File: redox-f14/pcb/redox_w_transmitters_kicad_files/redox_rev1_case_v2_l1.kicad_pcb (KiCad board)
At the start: 2 copper layers, 164.3 x 134.8 mm, 0 parts

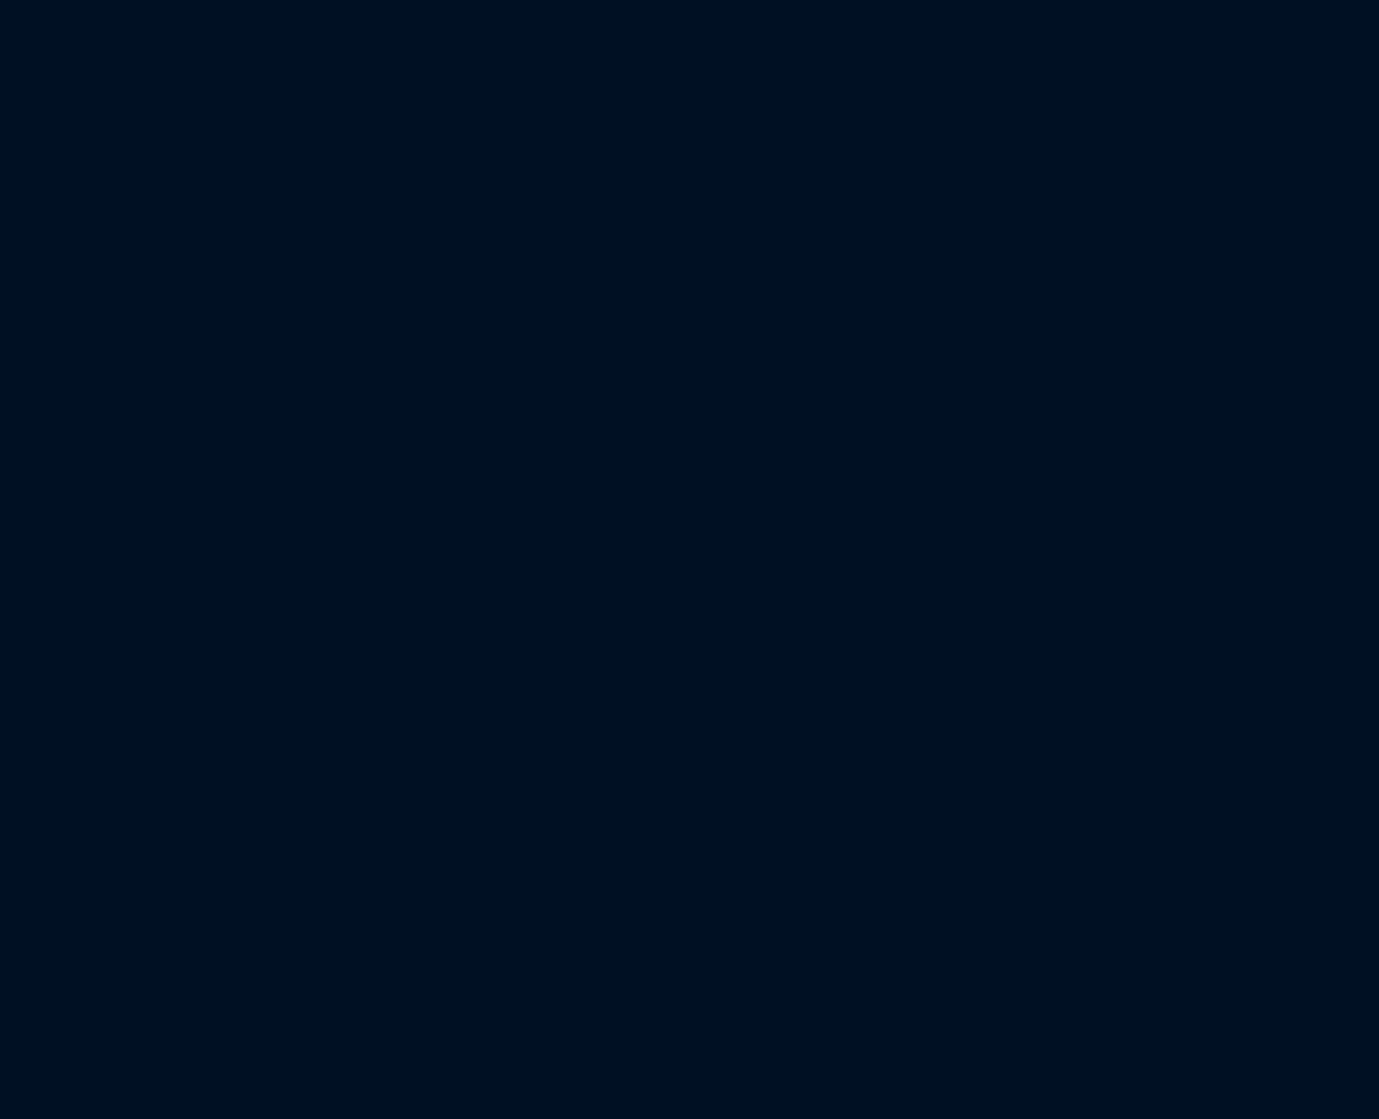
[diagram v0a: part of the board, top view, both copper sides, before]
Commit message: wingxx case update
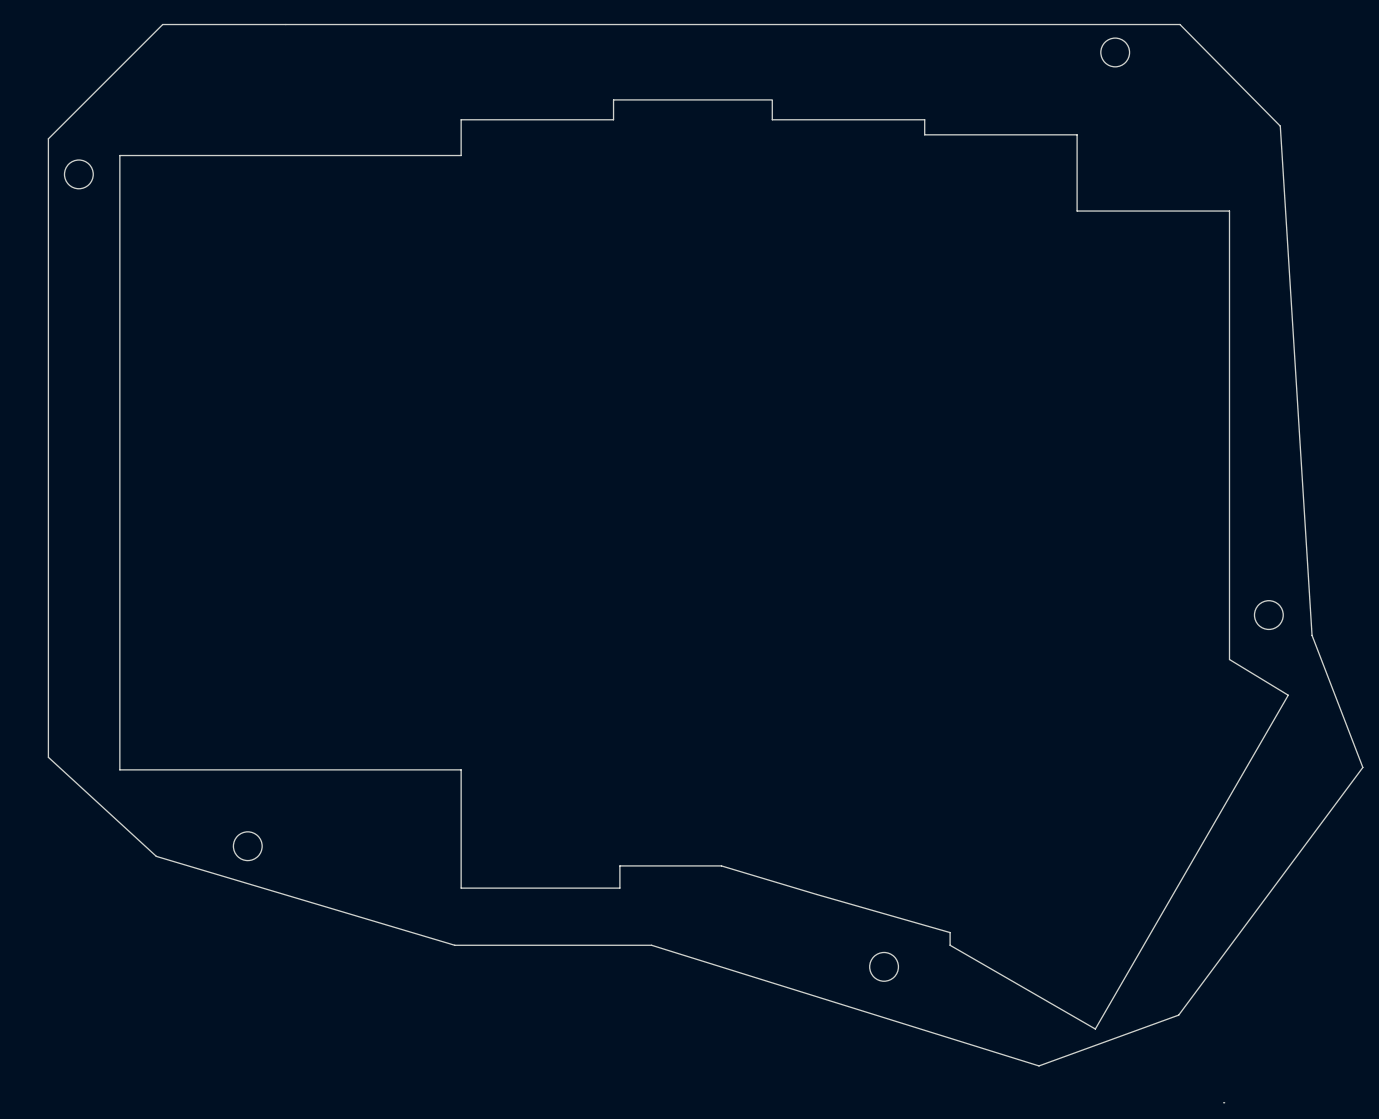
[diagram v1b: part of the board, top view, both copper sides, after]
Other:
- board size 164.3 x 134.8 mm -> 377.9 x 135.8 mm
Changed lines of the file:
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@@
   (general
     (thickness 1.6)
-    (drawings 43)
+    (drawings 86)
     (tracks 0)
     (zones 0)
@@
     (visible_elements 7FFFFFFF)
     (pcbplotparams
-      (layerselection 0x010fc_ffffffff)
+      (layerselection 0x01000_7ffffffe)
       (usegerberextensions true)
       (usegerberattributes false)
       (usegerberadvancedattributes false)
       (creategerberjobfile false)
-      (excludeedgelayer true)
+      (excludeedgelayer false)
       (linewidth 0.100000)
       (plotframeref false)
@@
       (psnegative false)
       (psa4output false)
-      (plotreference true)
-      (plotvalue true)
+      (plotreference false)
+      (plotvalue false)
       (plotinvisibletext false)
-      (padsonsilk false)
+      (padsonsilk true)
       (subtractmaskfromsilk false)
-      (outputformat 1)
+      (outputformat 3)
       (mirror false)
       (drillshape 0)
       (scaleselection 1)
-      (outputdirectory "gerber_files/"))
+      (outputdirectory "dxf/"))
   )
   (net 0 "")
@@
     (uvia_drill 0.1)
   )
+  (gr_circle (center 417.60775 44.98975) (end 418.87775 46.25975) (layer Edge.Cuts) (width 0.1))
+  (gr_circle (center 436.8165 115.316) (end 438.0865 116.586) (layer Edge.Cuts) (width 0.1))
+  (gr_circle (center 388.71525 159.28975) (end 389.98525 160.55975) (layer Edge.Cuts) (width 0.1))
+  (gr_circle (center 309.1815 144.2085) (end 310.4515 145.4785) (layer Edge.Cuts) (width 0.1))
+  (gr_circle (center 288.06775 60.22975) (end 289.33775 61.49975) (layer Edge.Cuts) (width 0.1))
+  (gr_line (start 354.9015 53.4035) (end 354.9015 50.92225) (layer Edge.Cuts) (width 0.1))
+  (gr_line (start 284.25775 55.78475) (end 284.25775 133.096) (layer Edge.Cuts) (width 0.1))
+  (gr_line (start 293.189 57.87225) (end 335.8515 57.87225) (layer Edge.Cuts) (width 0.1))
+  (gr_line (start 374.74525 51.02225) (end 374.74525 53.4035) (layer Edge.Cuts) (width 0.1))
+  (gr_line (start 335.8515 134.666) (end 293.189 134.666) (layer Edge.Cuts) (width 0.1))
+  (gr_line (start 412.84525 55.28475) (end 412.84525 64.80975) (layer Edge.Cuts) (width 0.1))
+  (gr_line (start 335.05775 156.591) (end 297.7515 145.4785) (layer Edge.Cuts) (width 0.1))
+  (gr_line (start 380.3015 150.241) (end 368.39525 146.67225) (layer Edge.Cuts) (width 0.1))
+  (gr_line (start 297.7515 145.4785) (end 284.25775 133.096) (layer Edge.Cuts) (width 0.1))
+  (gr_line (start 284.25775 55.78475) (end 298.54525 41.49725) (layer Edge.Cuts) (width 0.1))
+  (gr_line (start 355.69525 149.44725) (end 355.69525 146.67225) (layer Edge.Cuts) (width 0.1))
+  (gr_line (start 380.3015 150.241) (end 396.97025 155.0035) (layer Edge.Cuts) (width 0.1))
+  (gr_line (start 374.74525 53.4035) (end 393.79525 53.4035) (layer Edge.Cuts) (width 0.1))
+  (gr_line (start 335.8515 149.44725) (end 355.69525 149.44725) (layer Edge.Cuts) (width 0.1))
+  (gr_line (start 293.189 134.666) (end 293.189 57.87225) (layer Edge.Cuts) (width 0.1))
+  (gr_line (start 354.9015 50.92225) (end 374.74525 50.92225) (layer Edge.Cuts) (width 0.1))
+  (gr_line (start 335.8515 57.87225) (end 335.8515 53.4035) (layer Edge.Cuts) (width 0.1))
+  (gr_line (start 393.79525 55.28475) (end 393.79525 53.4035) (layer Edge.Cuts) (width 0.1))
+  (gr_line (start 335.8515 53.4035) (end 354.9015 53.4035) (layer Edge.Cuts) (width 0.1))
+  (gr_line (start 335.8515 149.44725) (end 335.8515 134.666) (layer Edge.Cuts) (width 0.1))
+  (gr_line (start 393.79525 55.28475) (end 412.84525 55.28475) (layer Edge.Cuts) (width 0.1))
+  (gr_line (start 425.54525 165.32225) (end 408.08275 171.67225) (layer Edge.Cuts) (width 0.1))
+  (gr_line (start 408.08275 171.67225) (end 359.664 156.591) (layer Edge.Cuts) (width 0.1))
+  (gr_line (start 359.664 156.591) (end 335.05775 156.591) (layer Edge.Cuts) (width 0.1))
+  (gr_line (start 355.69525 146.67225) (end 368.39525 146.67225) (layer Edge.Cuts) (width 0.1))
+  (gr_line (start 442.214 117.856) (end 448.564 134.366) (layer Edge.Cuts) (width 0.1))
+  (gr_line (start 448.564 134.366) (end 425.54525 165.32225) (layer Edge.Cuts) (width 0.1))
+  (gr_line (start 438.24525 54.19725) (end 442.214 117.856) (layer Edge.Cuts) (width 0.1))
+  (gr_line (start 431.165 176.276) (end 431.292 176.276) (angle 90) (layer Edge.Cuts) (width 0.1))
+  (gr_line (start 425.704 41.49725) (end 438.24525 54.19725) (layer Edge.Cuts) (width 0.1))
+  (gr_line (start 298.54525 41.49725) (end 313.944 41.49725) (layer Edge.Cuts) (width 0.1))
+  (gr_line (start 313.944 41.49725) (end 425.704 41.49725) (layer Edge.Cuts) (width 0.1))
+  (gr_line (start 415.1265 167.05975) (end 396.97025 156.591) (layer Edge.Cuts) (width 0.1))
+  (gr_line (start 396.97025 156.591) (end 396.97025 155.0035) (layer Edge.Cuts) (width 0.1))
+  (gr_line (start 412.84525 64.80975) (end 431.89525 64.80975) (layer Edge.Cuts) (width 0.1))
+  (gr_line (start 431.89525 64.80975) (end 431.89525 120.87225) (layer Edge.Cuts) (width 0.1))
+  (gr_line (start 431.89525 120.87225) (end 439.239 125.33475) (layer Edge.Cuts) (width 0.1))
+  (gr_line (start 439.239 125.33475) (end 415.1265 167.05975) (layer Edge.Cuts) (width 0.1))
   (gr_circle (center 203.99375 43.97375) (end 205.26375 43.97375) (layer Edge.Cuts) (width 0.1))
   (gr_circle (center 74.45375 59.21375) (end 75.72375 59.21375) (layer Edge.Cuts) (width 0.1))
